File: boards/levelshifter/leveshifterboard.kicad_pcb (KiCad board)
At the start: 2 copper layers, 82.5 x 43.2 mm, 49 parts, among them J1 RJ45, P1 CONN_2, P2 CONN_7, Q2 NDS355, SW1 SW_PUSH, U1 LM358, U2 74HC74, U3 74HCT125, U4 TS2937, U5 BTS462

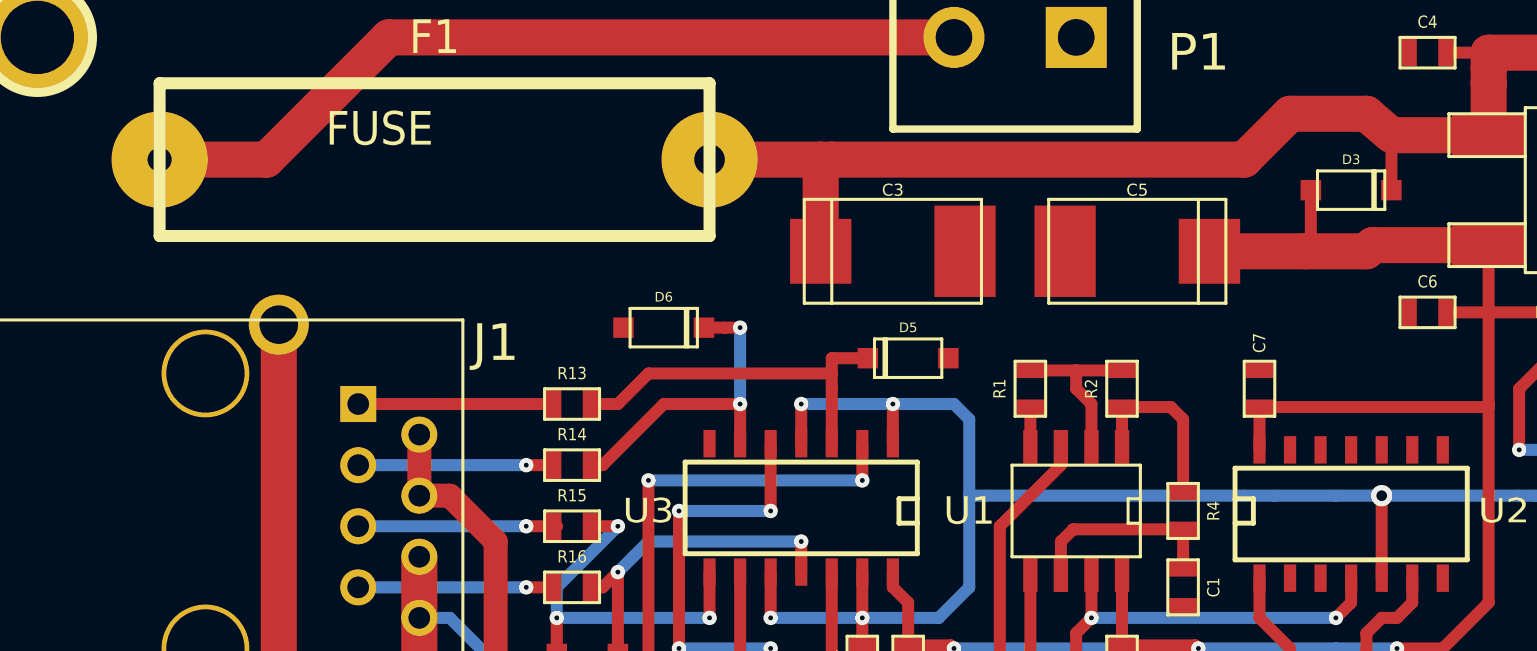
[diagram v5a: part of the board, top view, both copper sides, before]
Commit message: Updated resistor values
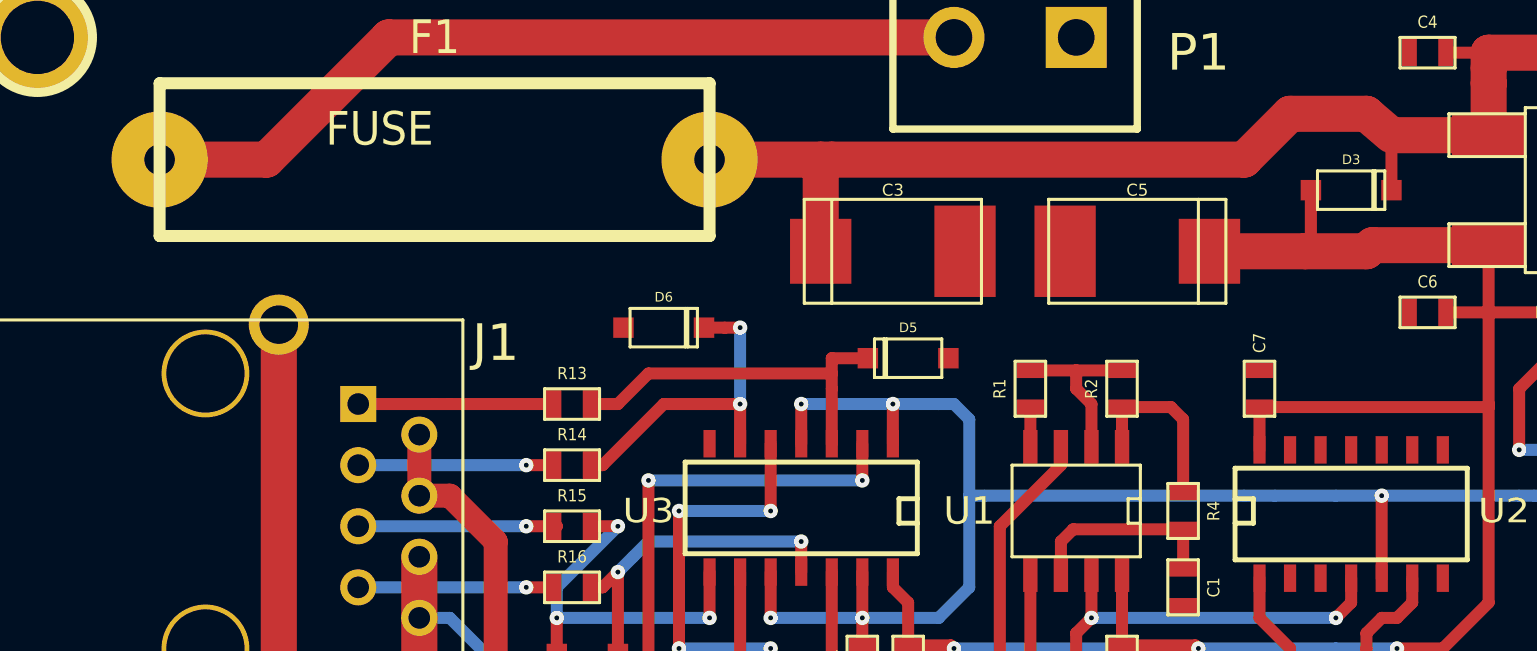
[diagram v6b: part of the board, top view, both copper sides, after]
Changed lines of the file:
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@@
     (mod_text_width 0.15)
     (pad_size 4.0005 4.0005)
-    (pad_drill 1.00076)
+    (pad_drill 1.27)
     (pad_to_mask_clearance 0)
     (aux_axis_origin 0 0)
@@
     (fp_line (start -11.43 -3.175) (end 11.43 -3.175) (layer F.SilkS) (width 0.15))
     (fp_line (start 11.43 -3.175) (end 11.43 3.175) (layer F.SilkS) (width 0.15))
-    (pad 1 thru_hole circle (at -11.43 0) (size 4.0005 4.0005) (drill 1.00076)
+    (pad 1 thru_hole circle (at -11.43 0) (size 4.0005 4.0005) (drill 1.27)
       (layers *.Cu *.Mask F.SilkS)
       (net 22 N-0000029)
@@
   (segment (start 155.575 81.28) (end 155.575 70.485) (width 0.5) (layer F.Cu) (net 7) (status 10))
   (segment (start 178.435 70.739) (end 178.435 67.31) (width 0.5) (layer F.Cu) (net 8))
-  (via (at 178.435 67.31) (size 0.889) (layers F.Cu B.Cu) (net 8))
+  (via (at 178.435 67.31) (size 0.6) (drill 0.2) (layers F.Cu B.Cu) (net 8) (status 1000000))
   (segment (start 172.72 67.31) (end 161.925 67.31) (width 0.5) (layer B.Cu) (net 8))
   (segment (start 156.845 72.39) (end 156.845 73.533) (width 0.5) (layer F.Cu) (net 8))
